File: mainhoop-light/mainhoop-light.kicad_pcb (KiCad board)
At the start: 2 copper layers, 74 x 57 mm, 74 parts, among them IC1 BCR420U, IC3 BCR420U, IC4 BCR420U, IC5 BCR420U, IC6 BCR420U, J1 Conn_01x04, Q1 2N7002, Q12 Si2301CDS, Q13 2N7002, Q14 2N7002, Q15 Si2301CDS, Q16 2N7002, Q2 2N7002, Q3 Si2301CDS, Q7 2N7002, U1 AP2204K-ADJ, U2 SE555D

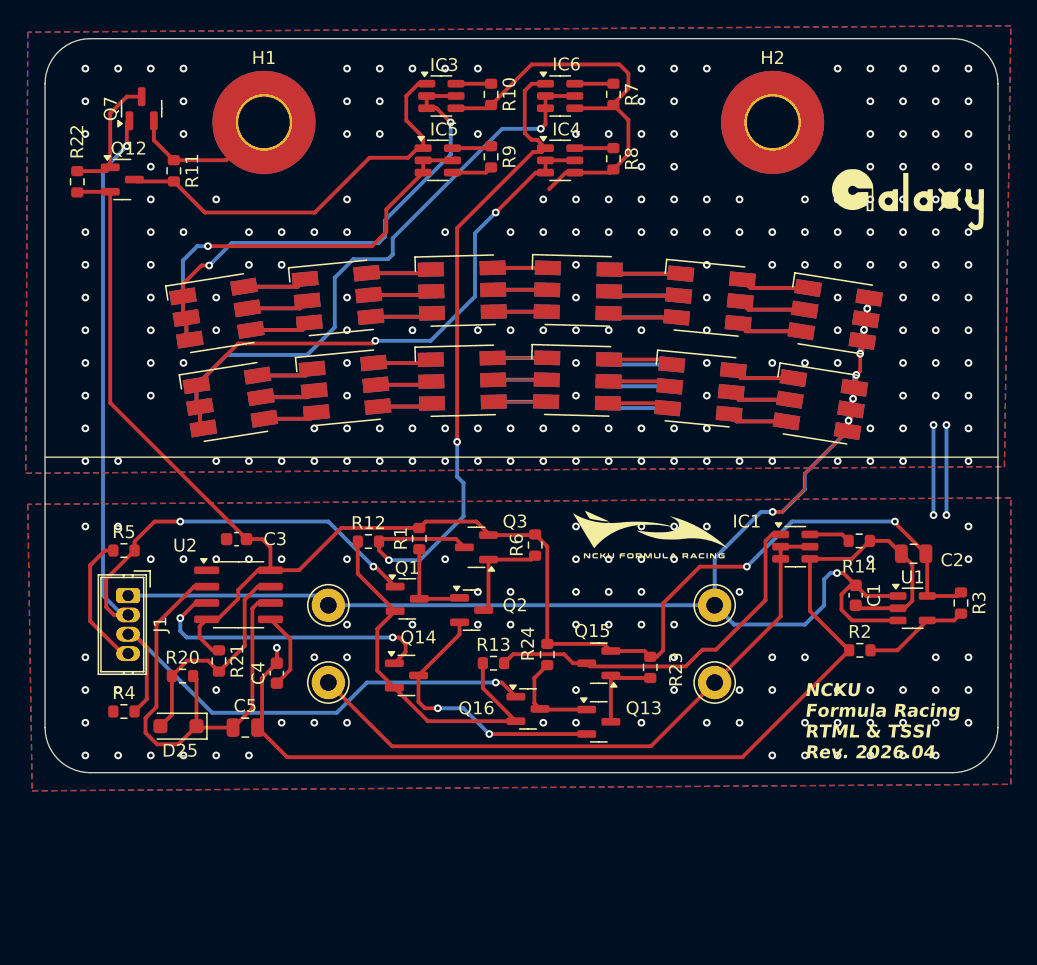
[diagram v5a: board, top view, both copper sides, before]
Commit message: fix: replace PMOS, resistor and pull-up of RTML
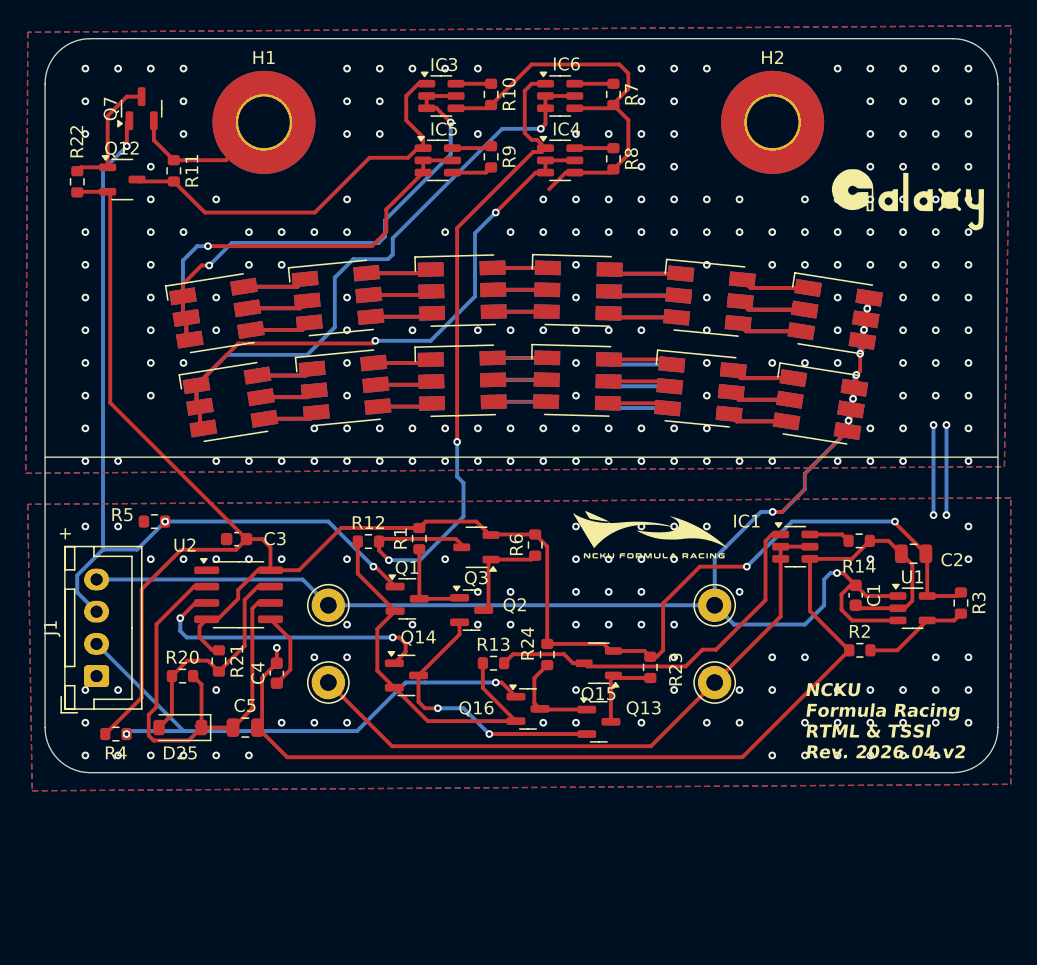
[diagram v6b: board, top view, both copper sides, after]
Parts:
- D25: value D_Small -> 1N4148W; footprint Diode_SMD:D_SOD-123F -> Diode_SMD:D_SOD-123
- J1: footprint Connector_Wuerth:Wuerth_WR-WTB_64800411622_1x04_P1.50mm_Vertical -> Connector_JST:JST_XH_B4B-XH-A_1x04_P2.50mm_Vertical
- Q12, Q15, Q3: value Si2301CDS -> NXV90EPR; footprint Package_TO_SOT_SMD:SOT-23 -> Package_TO_SOT_SMD:SOT-23-3
- R10, R7, R8, R9: value 15R -> 30R
- R14: value ~ -> 30R
- moved J1 6.71 mm to (66.0, 71.5), turned to 90 degrees
- moved R5 3.27 mm to (70.5, 59.5)
- moved R4 1.86 mm to (67.5, 76.0)
- moved D25 0.18 mm to (72.5, 75.5)
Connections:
- J1 pad 1: VDC -> GND
- J1 pad 2: TSSI -> RTML
- J1 pad 3: RTML -> TSSI
- J1 pad 4: GND -> VDC
- R4 pad 1: +5V -> +12V
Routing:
- net +12V: track 123.3 -> 145.5 mm
- net GND: track 184.5 -> 173.9 mm, vias 273 -> 272
- net TSSI: track 71.7 -> 66.1 mm
- net VDC: track 119.2 -> 122.2 mm
- net RTML: track 41.3 -> 41.9 mm, vias 1 -> 2
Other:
- board text added: "+"
- board text added: "NCKU Formula Racing RTML & TSSI Rev. 2026.04.v2"
- board text removed: "NCKU Formula Racing RTML & TSSI Rev. 2026.04"
